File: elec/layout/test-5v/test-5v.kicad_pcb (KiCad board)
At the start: 2 copper layers, 8 parts, among them U3 10µH ±20%

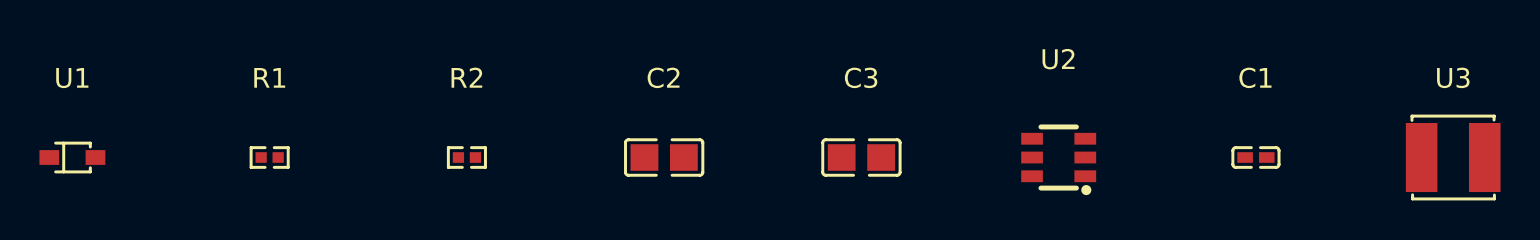
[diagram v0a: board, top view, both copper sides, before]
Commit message: Update layouts to kicad 9, add default build for layout reuse
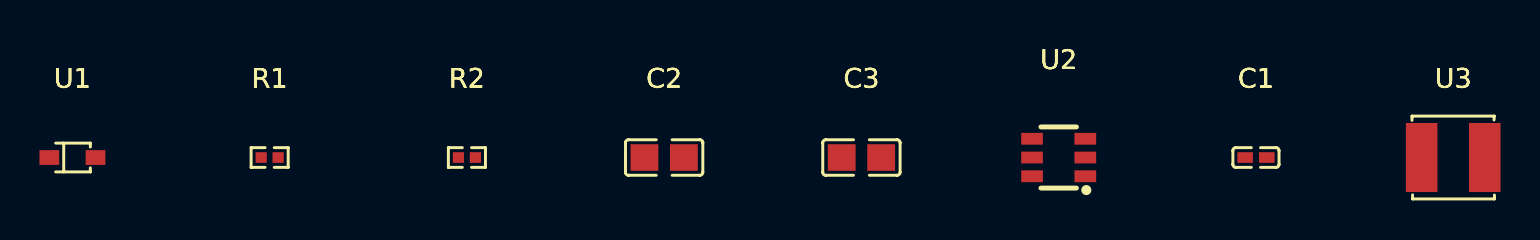
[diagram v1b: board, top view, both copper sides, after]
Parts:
- C2: value 10µF ±10% 25V X5R -> 4.7µF ±10% 25V X5R
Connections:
- net line renamed FB
- C2 pad 1: hv -> hv-1
- C3 pad 1: hv-1 -> hv
- R2 pad 1: hv-1 -> hv
- U2 pad 4: hv -> hv-1
- U2 pad 5: hv -> hv-1
- U3 pad 2: hv-1 -> hv
